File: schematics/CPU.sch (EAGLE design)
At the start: 17 parts, among them J5 EXPANSION_EDGE, J6 CARTRIDGE_CONNECTOR, U1 UM62256, U2 UM62256, U9 MC68HC000P10

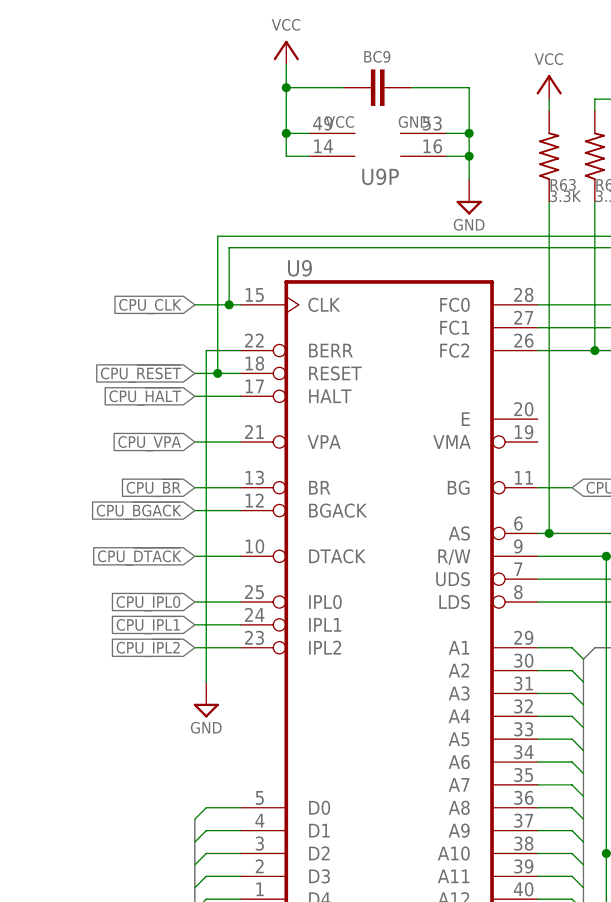
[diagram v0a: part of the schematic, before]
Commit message: Correct CPU BERR signal
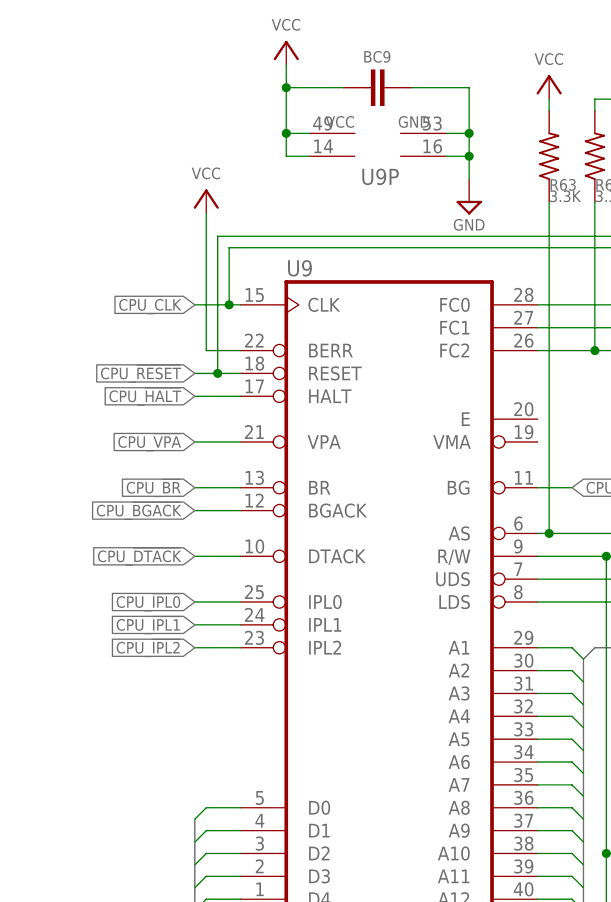
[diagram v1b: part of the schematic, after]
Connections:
- net GND: no longer U9G$1.BERR
- net VCC: now also U9G$1.BERR
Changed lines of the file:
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@@
 <?xml version="1.0" encoding="utf-8"?>
 <!DOCTYPE eagle SYSTEM "eagle.dtd">
-<eagle version="9.5.1">
+<eagle version="9.6.1">
 <drawing>
 <settings>
@@
 <setting verticaltext="up"/>
 </settings>
-<grid distance="0.1" unitdist="inch" unit="inch" style="lines" multiple="1" display="no" altdistance="0.01" altunitdist="inch" altunit="inch"/>
+<grid distance="0.05" unitdist="inch" unit="inch" style="lines" multiple="1" display="yes" altdistance="0.01" altunitdist="inch" altunit="inch"/>
 <layers>
 <layer number="1" name="Top" color="4" fill="1" visible="no" active="no"/>
@@
 <part name="P+1" library="supply1" library_urn="urn:adsk.eagle:library:371" deviceset="VCC" device=""/>
 <part name="SUPPLY10" library="supply2" library_urn="urn:adsk.eagle:library:372" deviceset="GND" device=""/>
-<part name="SUPPLY11" library="supply2" library_urn="urn:adsk.eagle:library:372" deviceset="GND" device=""/>
+<part name="P+9" library="supply1" library_urn="urn:adsk.eagle:library:371" deviceset="VCC" device=""/>
 </parts>
 <sheets>
@@
 <attribute name="VALUE" x="49.53" y="186.055" size="1.27" layer="96" align="top-center"/>
 </instance>
-<instance part="SUPPLY11" gate="GND" x="20.32" y="132.08" smashed="yes">
-<attribute name="VALUE" x="20.32" y="130.175" size="1.27" layer="96" align="top-center"/>
+<instance part="P+9" gate="VCC" x="20.32" y="189.23" smashed="yes">
+<attribute name="VALUE" x="20.32" y="190.5" size="1.27" layer="96" align="bottom-center"/>
 </instance>
 </instances>
@@
 <junction x="29.21" y="200.66"/>
 </segment>
+<segment>
+<pinref part="U9" gate="G$1" pin="BERR"/>
+<wire x1="24.13" y1="171.45" x2="20.32" y2="171.45" width="0.1524" layer="91"/>
+<wire x1="20.32" y1="171.45" x2="20.32" y2="186.69" width="0.1524" layer="91"/>
+<pinref part="P+9" gate="VCC" pin="VCC"/>
+</segment>
 </net>
 <net name="CPU_FC0" class="0">
@@
 <pinref part="SUPPLY10" gate="GND" pin="GND"/>
 </segment>
-<segment>
-<pinref part="U9" gate="G$1" pin="BERR"/>
-<wire x1="24.13" y1="171.45" x2="20.32" y2="171.45" width="0.1524" layer="91"/>
-<wire x1="20.32" y1="171.45" x2="20.32" y2="134.62" width="0.1524" layer="91"/>
-<pinref part="SUPPLY11" gate="GND" pin="GND"/>
-</segment>
 </net>
